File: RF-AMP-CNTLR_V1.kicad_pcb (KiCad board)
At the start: 4 copper layers, 220 x 100 mm, 324 parts, among them J1 VAC, J10 FWD3, J11 REF3, J12 FWD4, J13 REF4, J14 ALC, J15 AMP1, J16 AMP2, J17 FAN, J18 PTT, J19 FRONT PANEL, J2 VDC, J20 GPIO, J21 I2C, J22 UART, J23 Conn_02x03_Odd_Even, J24 ICSP, J25 Raspberry_Pi_2_3, J3 ext_13V8, J4 VDD IN, J5 VSS IN, J6 VDD OUT, J7 VSS OUT, J8 RF SWITCH AMP OUT, J9 RF SWITCH AMP IN, Q1 BC857, Q10 BCX53, Q11 BCX53, Q12 BCX53, Q13 DTC124E, Q14 DTC124E, Q15 DTC124E, Q16 DTC124E, Q17 DTC124E, Q18 BCX53, Q2 IXTH140P10T, Q3 DTC124E, Q4 IXTH140P10T, Q5 DTA124E, Q6 DTC124E, Q7 DTC124E, Q8 DTC124E, Q9 BCX53, U1 L7812, U10 74LVC2G17, U11 CD4052B, U12 74LVC2G14, U13 74LVC2G14, U14 ATmega8-16AU, U15 SN74LVC1G11DBVR, U16 SN74LVC1G11DBVR, U17 MCP23017_SO, U18 MAX11616, U19 TXS0108EPW, U2 NCS20072D, U20 TXS0108EPW, U21 TXS0108EPW, U22 MCP23017_SO, U23 MAX3232, U3 NCS20074D, U4 INA138, U5 LM339, U6 NCS20074D, U7 NCS20072D, U8 LM339, U9 74LVC2G17

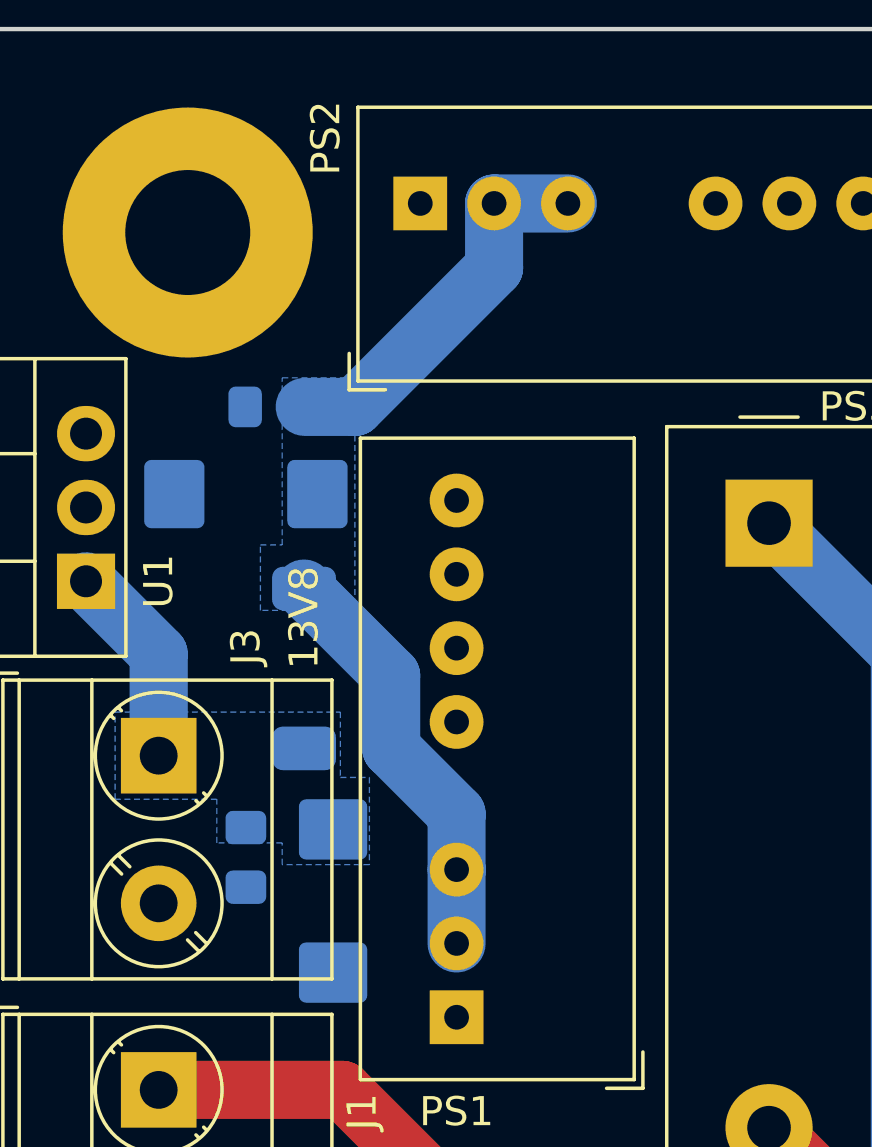
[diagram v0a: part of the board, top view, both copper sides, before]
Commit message: bug fix ITQ ON/OFF
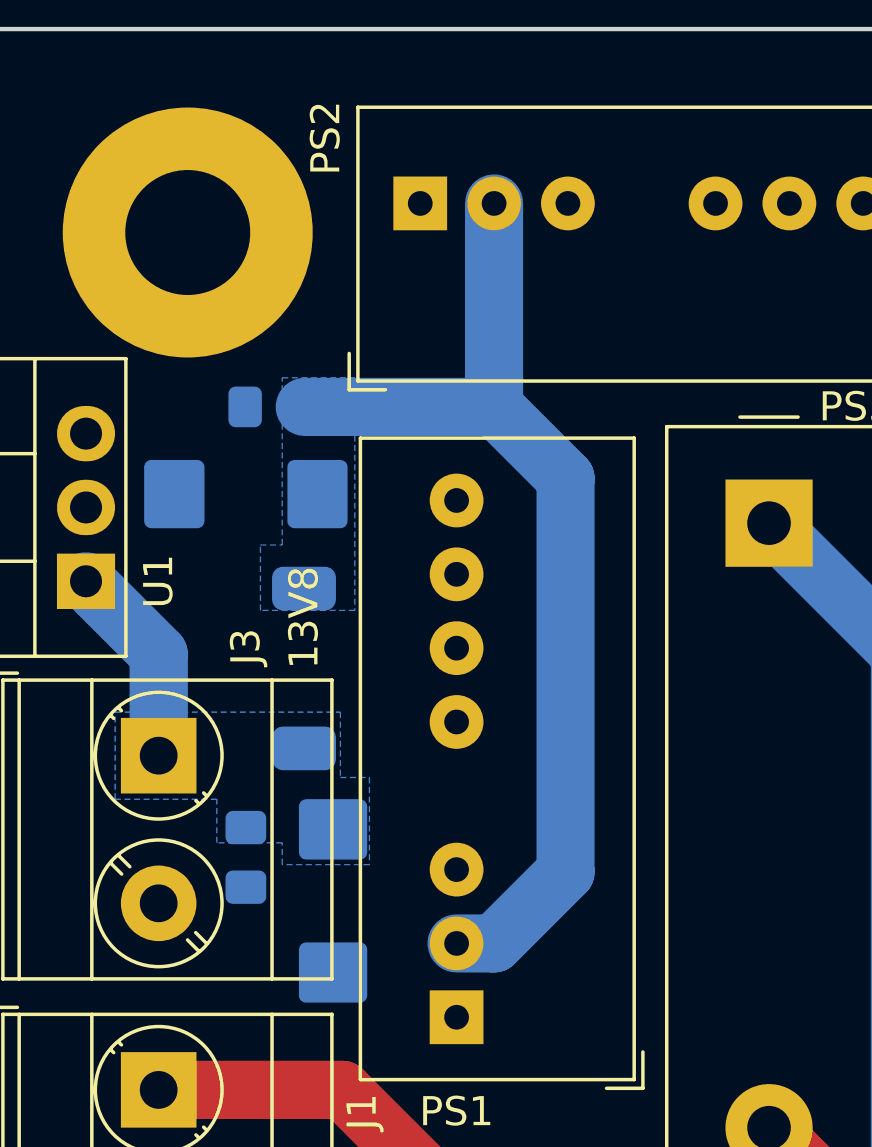
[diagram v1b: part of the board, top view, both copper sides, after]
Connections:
- PS1 pad 3: Net-(C4-Pad1) -> Earth
- PS2 pad 3: Net-(C4-Pad1) -> Earth
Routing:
- net Net-(C4-Pad1): track 27.6 -> 35.3 mm

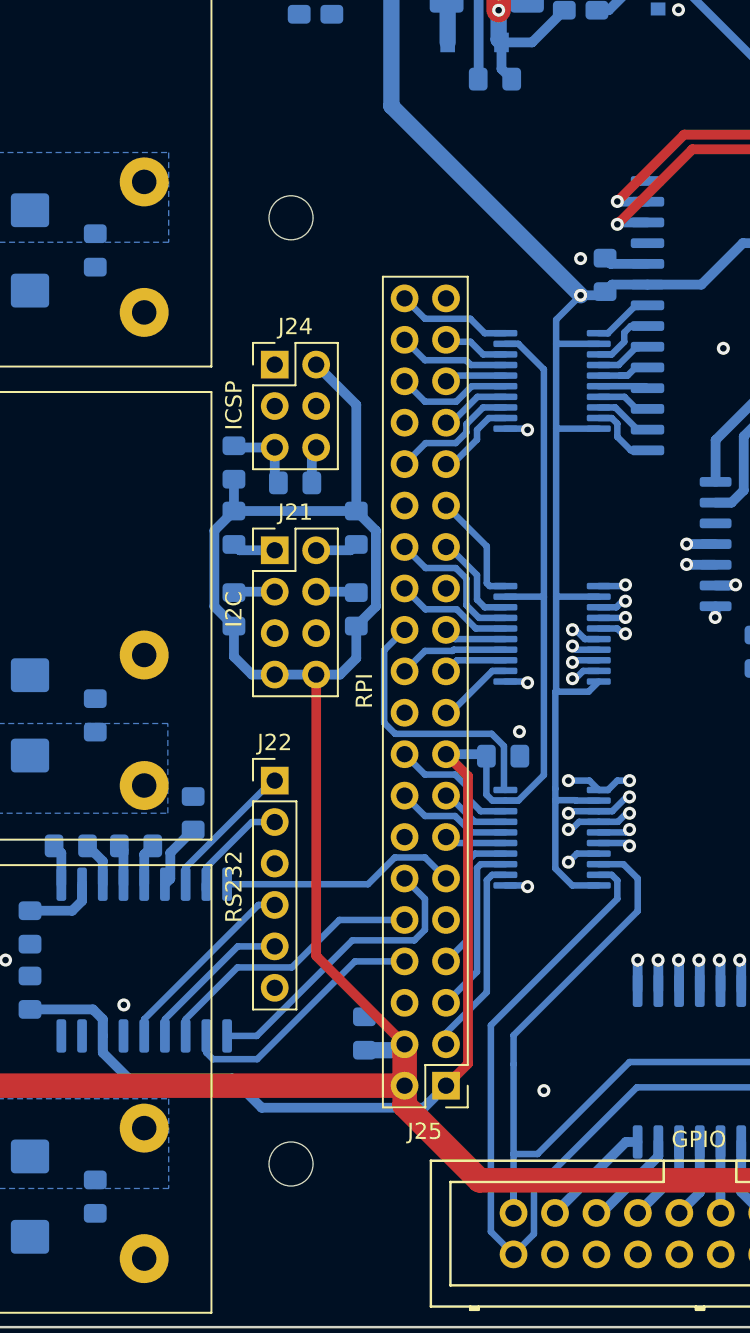
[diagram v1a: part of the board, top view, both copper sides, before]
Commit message: bug fix level shifter U19-U21 VCCA VCCB swap
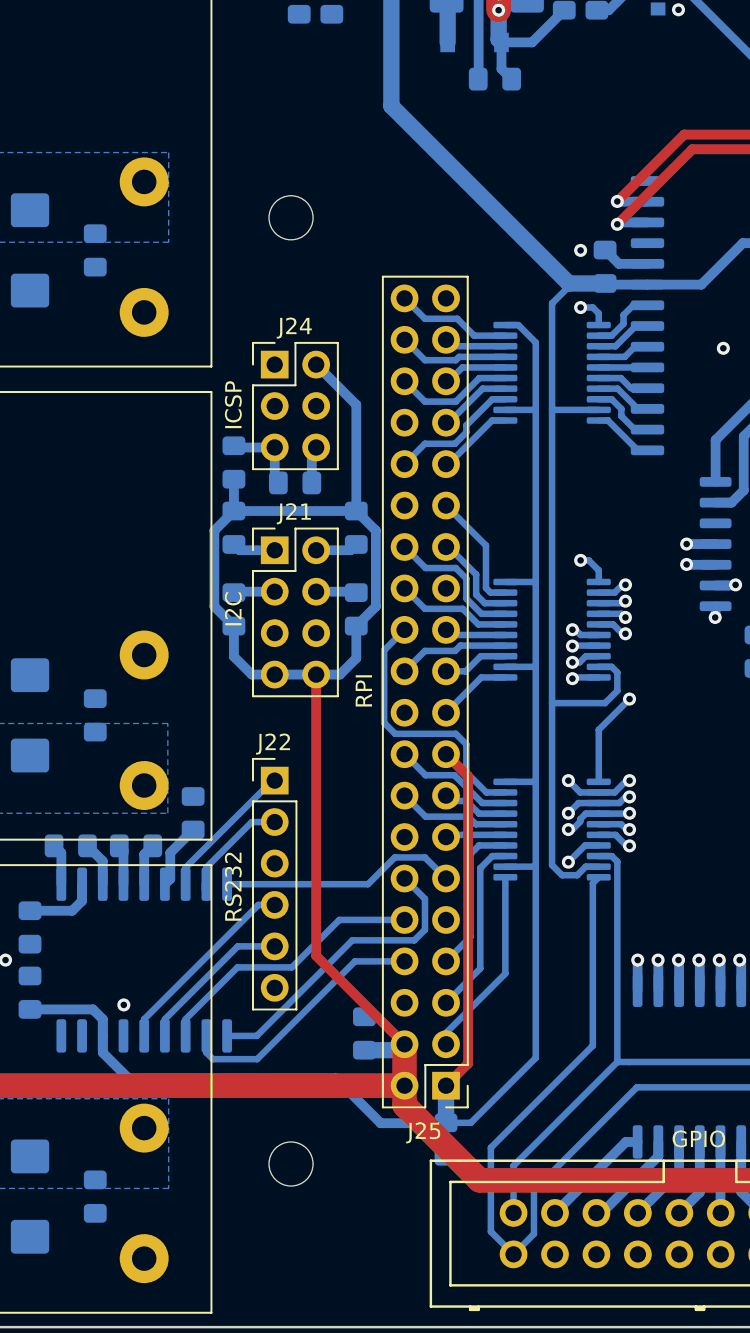
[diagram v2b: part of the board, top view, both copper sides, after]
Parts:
- moved C78 23.8 mm to (110.5, 138.5), turned to 270 degrees
- moved C75 0.50 mm to (120.2, 85.0)
- moved U20 0.50 mm to (117.0, 91.5), turned to 0 degrees
- moved U21 0.50 mm to (117.0, 119.5), turned to 0 degrees
- moved U19 0.25 mm to (117.0, 107.2), turned to 0 degrees
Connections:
- U19 pad 1: /CONTROLLER/RESET_ILK -> /CONTROLLER/MOSI_FAN_LV
- U19 pad 10: +5V -> +3V3
- U19 pad 12: /CONTROLLER/MOSI_FAN_LV -> /CONTROLLER/RESET_ILK
- U19 pad 13: /CONTROLLER/MISO_RF_INHIBIT_LV -> /CONTROLLER/DISPLAY
- U19 pad 14: /CONTROLLER/RESET_ISP_LV -> /CONTROLLER/PTT
- U19 pad 15: /CONTROLLER/SCK_SOFT_ILK_LV -> /CONTROLLER/OPR
- U19 pad 16: /CONTROLLER/OPR_LV -> /CONTROLLER/SCK_SOFT_ILK
- U19 pad 17: /CONTROLLER/PTT_LV -> /CONTROLLER/RESET_ISP
- U19 pad 18: /CONTROLLER/DISPLAY_LV -> /CONTROLLER/MISO_RF_INHIBIT
- U19 pad 19: +3V3 -> +5V
- U19 pad 2: +5V -> +3V3
- U19 pad 20: /CONTROLLER/RESET_ILK_LV -> /CONTROLLER/MOSI_FAN
- U19 pad 3: /CONTROLLER/DISPLAY -> /CONTROLLER/MISO_RF_INHIBIT_LV
- U19 pad 4: /CONTROLLER/PTT -> /CONTROLLER/RESET_ISP_LV
- U19 pad 5: /CONTROLLER/OPR -> /CONTROLLER/SCK_SOFT_ILK_LV
- U19 pad 6: /CONTROLLER/SCK_SOFT_ILK -> /CONTROLLER/OPR_LV
- U19 pad 7: /CONTROLLER/RESET_ISP -> /CONTROLLER/PTT_LV
- U19 pad 8: /CONTROLLER/MISO_RF_INHIBIT -> /CONTROLLER/DISPLAY_LV
- U19 pad 9: /CONTROLLER/MOSI_FAN -> /CONTROLLER/RESET_ILK_LV
- U20 pad 1: /CONTROLLER/TEMP -> /CONTROLLER/HSWR1_LV
- U20 pad 10: +5V -> +3V3
- U20 pad 12: /CONTROLLER/HSWR1_LV -> /CONTROLLER/TEMP
- U20 pad 13: /CONTROLLER/HSWR2_LV -> /CONTROLLER/VDD_LIM
- U20 pad 14: /CONTROLLER/HSWR3_LV -> /CONTROLLER/IDD_OL
- U20 pad 15: /CONTROLLER/UNBAL_LV -> /CONTROLLER/RF_OL
- U20 pad 16: /CONTROLLER/RF_OL_LV -> /CONTROLLER/HSWR4
- U20 pad 17: /CONTROLLER/IDD_OL_LV -> /CONTROLLER/HSWR3
- U20 pad 18: /CONTROLLER/VDD_LIM_LV -> /CONTROLLER/HSWR2
- U20 pad 19: +3V3 -> +5V
- U20 pad 2: +5V -> +3V3
- U20 pad 20: /CONTROLLER/TEMP_LV -> /CONTROLLER/HSWR1
- U20 pad 3: /CONTROLLER/VDD_LIM -> /CONTROLLER/HSWR2_LV
- U20 pad 4: /CONTROLLER/IDD_OL -> /CONTROLLER/HSWR3_LV
- U20 pad 5: /CONTROLLER/RF_OL -> /CONTROLLER/UNBAL_LV
- U20 pad 6: /CONTROLLER/HSWR4 -> /CONTROLLER/RF_OL_LV
- U20 pad 7: /CONTROLLER/HSWR3 -> /CONTROLLER/IDD_OL_LV
- U20 pad 8: /CONTROLLER/HSWR2 -> /CONTROLLER/VDD_LIM_LV
- U20 pad 9: /CONTROLLER/HSWR1 -> /CONTROLLER/TEMP_LV
- U21 pad 1: /VDD_EN -> /CONTROLLER/SDA_PI_LV
- U21 pad 10: +5V -> +3V3
- U21 pad 12: /CONTROLLER/SDA_PI_LV -> /VDD_EN
- U21 pad 13: /CONTROLLER/SCL_PI_LV -> /RF_SW1_ON
- U21 pad 14: /CONTROLLER/FAULT_LV -> /RF_SW2_ON
- U21 pad 15: /CONTROLLER/ON_AIR_LV -> /GATE_ALC_EN
- U21 pad 16: /CONTROLLER/GATE_ALC_EN_LV -> /CONTROLLER/ON_AIR
- U21 pad 17: /CONTROLLER/RF_SW2_ON_LV -> /CONTROLLER/FAULT
- U21 pad 18: /CONTROLLER/RF_SW1_ON_LV -> /CONTROLLER/SCL_PI_HV
- U21 pad 19: +3V3 -> +5V
- U21 pad 2: +5V -> +3V3
- U21 pad 20: /CONTROLLER/VDD_EN_LV -> /CONTROLLER/SDA_PI_HV
- U21 pad 3: /RF_SW1_ON -> /CONTROLLER/SCL_PI_LV
- U21 pad 4: /RF_SW2_ON -> /CONTROLLER/FAULT_LV
- U21 pad 5: /GATE_ALC_EN -> /CONTROLLER/ON_AIR_LV
- U21 pad 6: /CONTROLLER/ON_AIR -> /CONTROLLER/GATE_ALC_EN_LV
- U21 pad 7: /CONTROLLER/FAULT -> /CONTROLLER/RF_SW2_ON_LV
- U21 pad 8: /CONTROLLER/SCL_PI_HV -> /CONTROLLER/RF_SW1_ON_LV
- U21 pad 9: /CONTROLLER/SDA_PI_HV -> /CONTROLLER/VDD_EN_LV
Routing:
- net +3V3: track 90.7 -> 116.0 mm
- net /CONTROLLER/SCL_PI_HV: track 146.5 -> 135.6 mm
- net Earth: track 109.9 -> 115.9 mm, vias 52 -> 50
- net +5V: track 877.7 -> 873.8 mm, vias 12 -> 11
- net /CONTROLLER/SDA_PI_HV: track 156.8 -> 155.2 mm
- net /CONTROLLER/HSWR2: track 3.49 -> 4.55 mm
- net /CONTROLLER/HSWR3: track 3.31 -> 4.14 mm
- net /CONTROLLER/SDA_PI_LV: track 12.4 -> 11.7 mm
- net /CONTROLLER/RF_SW1_ON_LV: track 8.02 -> 7.42 mm
- net /CONTROLLER/RF_OL: track 3.54 -> 2.99 mm
- net /CONTROLLER/VDD_LIM: track 4.60 -> 4.05 mm
- net /CONTROLLER/HSWR1: track 4.28 -> 3.75 mm

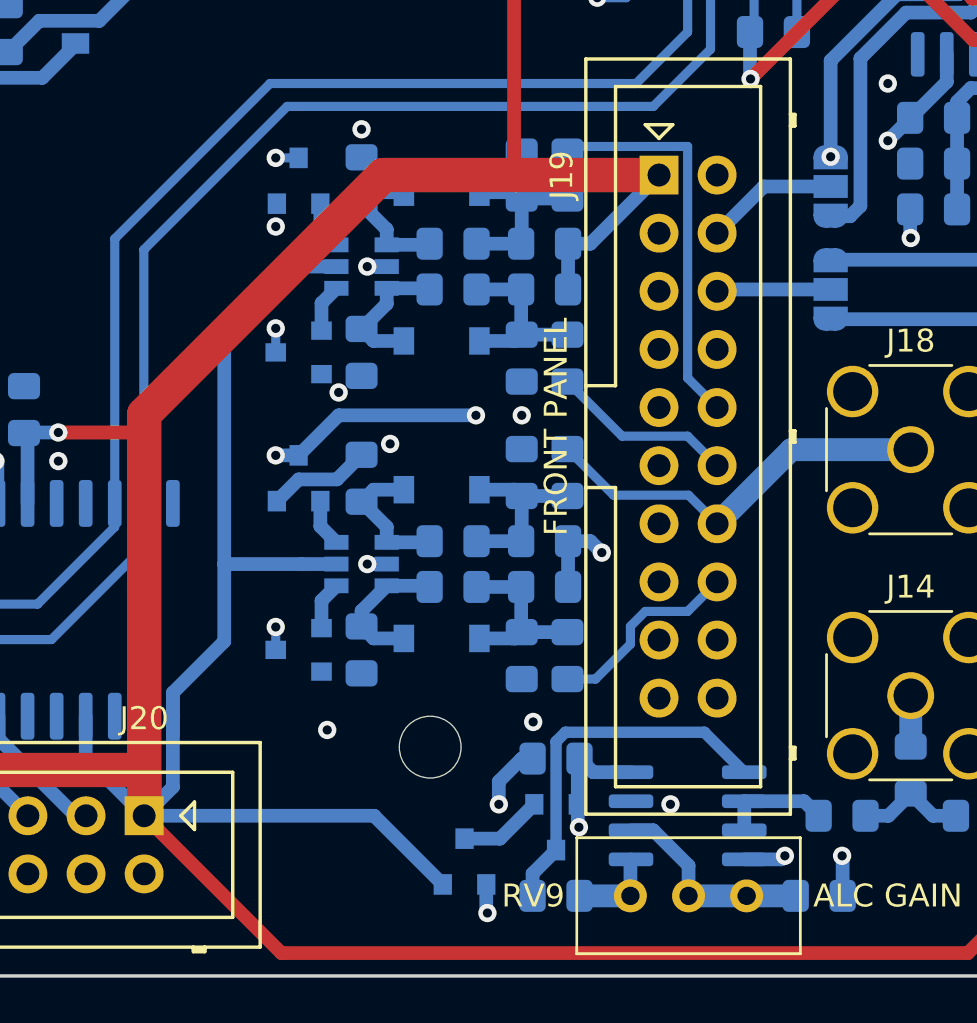
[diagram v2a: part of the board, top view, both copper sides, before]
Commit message: ALC latch-up fix
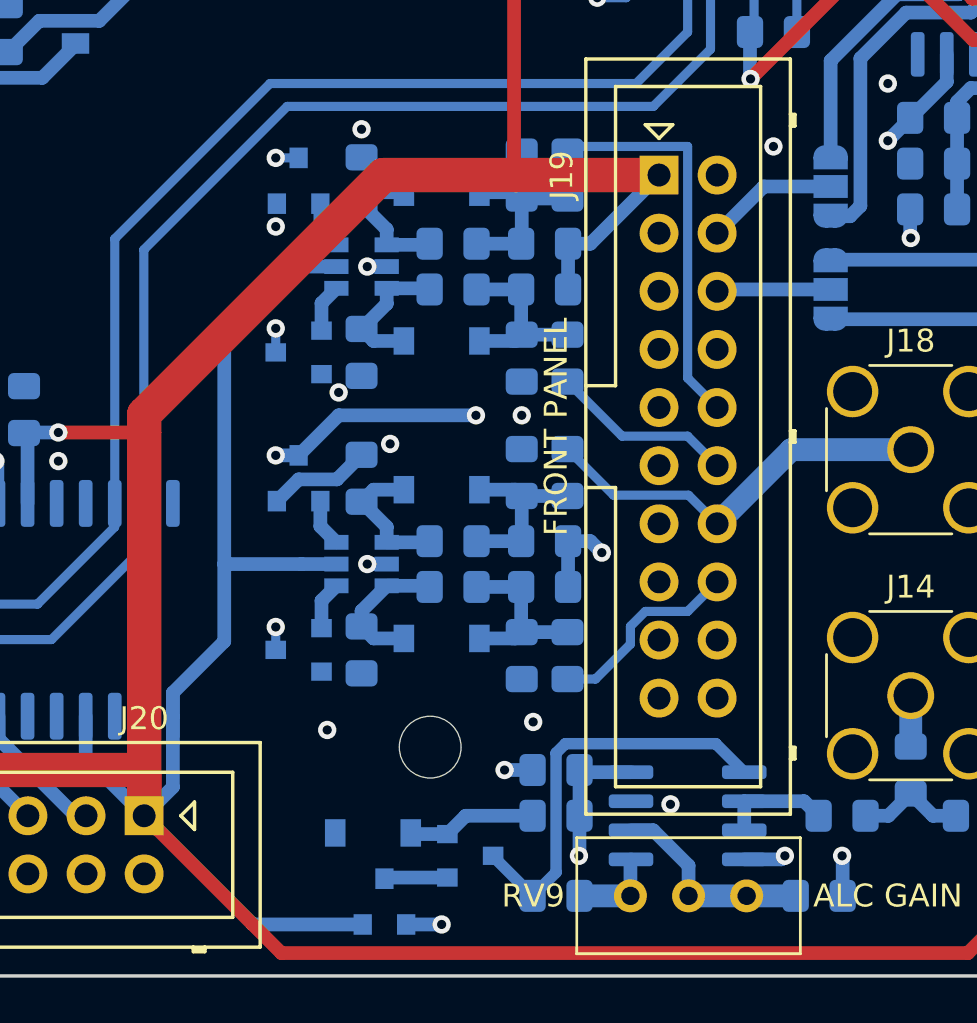
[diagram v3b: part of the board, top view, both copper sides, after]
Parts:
- added D19: BZT52C4V7T-7, Diode_SMD:D_SOD-123, B.Cu at (147.5, 143.8)
- added R103: 4k7, Resistor_SMD:R_0805_2012Metric_Pad1.15x1.40mm_HandSolder, B.Cu at (155.5, 143.0)
- R10: value 100k -> 68k
- R73: value 100k -> 470
- moved Q6 3.95 mm to (151.8, 144.8), turned to 0 degrees
- moved Q5 3.91 mm to (148.0, 146.8)
- moved C45 0.50 mm to (155.5, 141.0)
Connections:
- net Net-(J19-Pad6) renamed REF
- J19 pad 4: Net-(J19-Pad4) -> FWD
- JP1 pad 2: Net-(J19-Pad4) -> FWD
- Q6 pad 2: -12V -> Net-(D19-Pad2)
- R57 pad 2: /FWD4_MON -> FWD
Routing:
- net FWD: track 0.00 -> 39.2 mm, vias 0 -> 1
- net /FWD4_MON: track 75.0 -> 41.7 mm, vias 4 -> 2
- net Net-(J19-Pad4): track 5.80 -> 0.00 mm
- net Net-(D19-Pad2): track 0.00 -> 5.68 mm
- net +5V: track 873.8 -> 871.1 mm
- net /GATE_ALC_EN: track 213.9 -> 215.7 mm
- net Net-(Q6-Pad3): track 16.3 -> 18.0 mm
- net Net-(Q5-Pad3): track 3.67 -> 2.77 mm
- net Earth: vias 50 -> 51
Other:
- rule pad_to_mask_clearance: 0.051 -> 0
